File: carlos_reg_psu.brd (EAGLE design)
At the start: 51.7 x 40.6 mm, 17 parts

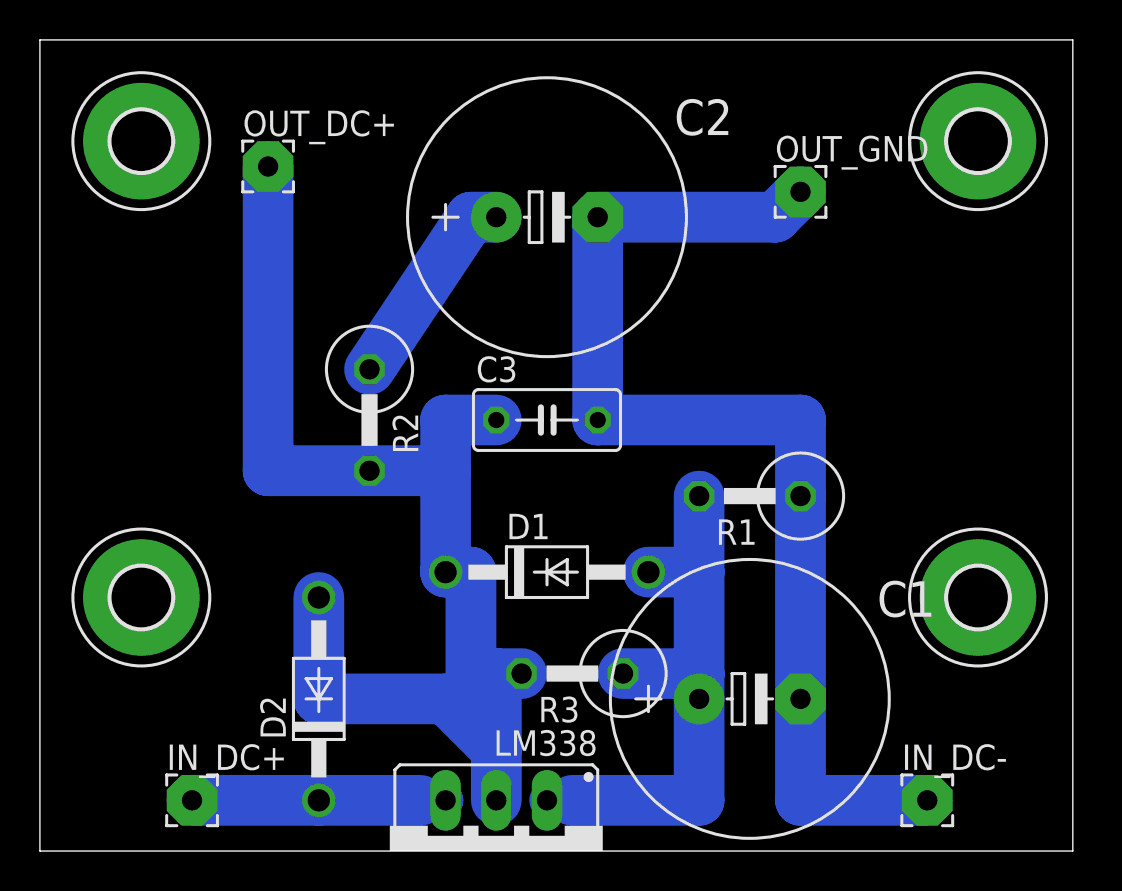
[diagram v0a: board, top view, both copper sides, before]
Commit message: minor placement fix
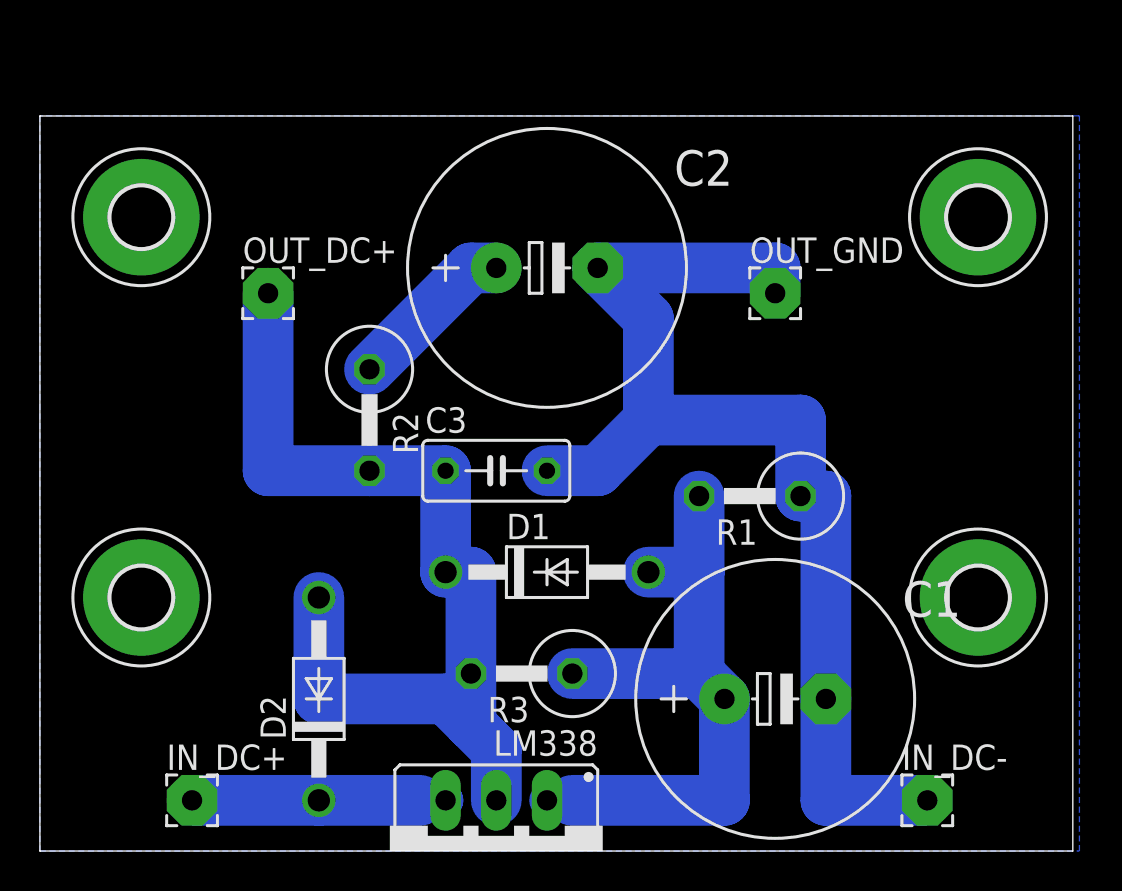
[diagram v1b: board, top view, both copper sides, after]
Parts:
- moved OUT_DC+ 6.35 mm to (11.4, 27.9)
- moved OUT_GND 5.24 mm to (36.8, 27.9)
- moved H3 3.81 mm to (47.0, 31.8)
- moved H4 3.81 mm to (5.08, 31.8)
- moved C3 3.59 mm to (22.9, 19.1)
- moved R3 2.54 mm to (24.1, 8.89)
- moved C2 2.54 mm to (25.4, 29.2)
- moved C1 1.27 mm to (36.8, 7.62)
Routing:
- net N$3: track 64.6 -> 49.3 mm
- net N$2: track 29.2 -> 33.5 mm
- net N$1: track 10.4 -> 8.45 mm
- net N$6: track 56.4 -> 58.0 mm
- added copper zone on layer 16, net GND
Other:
- board size 51.7 x 40.6 mm -> 51.7 x 36.8 mm
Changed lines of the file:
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@@
 <plain>
 <wire x1="0" y1="0" x2="51.74" y2="0" width="0" layer="20"/>
-<wire x1="51.74" y1="0" x2="51.74" y2="40.63" width="0" layer="20"/>
-<wire x1="51.74" y1="40.63" x2="0" y2="40.63" width="0" layer="20"/>
-<wire x1="0" y1="40.63" x2="0" y2="0" width="0" layer="20"/>
+<wire x1="51.74" y1="0" x2="51.74" y2="36.82" width="0" layer="20"/>
+<wire x1="51.74" y1="36.82" x2="0" y2="36.82" width="0" layer="20"/>
+<wire x1="0" y1="36.82" x2="0" y2="0" width="0" layer="20"/>
 </plain>
 <attributes>
@@
 </autorouter>
 <elements>
-<element name="C1" library="resistor" package="E5-13" value="47uF" x="35.56" y="7.62"/>
-<element name="C2" library="resistor" package="E5-13" value="47uF" x="25.4" y="31.75"/>
-<element name="C3" library="rcl" package="C050-030X075" value="47nF" x="25.4" y="21.59"/>
+<element name="C1" library="resistor" package="E5-13" value="47uF" x="36.83" y="7.62"/>
+<element name="C2" library="resistor" package="E5-13" value="47uF" x="25.4" y="29.21"/>
+<element name="C3" library="rcl" package="C050-030X075" value="47nF" x="22.86" y="19.05"/>
 <element name="D1" library="diode" package="DO41-10" value="1N4002" x="25.4" y="13.97"/>
 <element name="D2" library="diode" package="DO41-10" value="1N4002" x="13.97" y="7.62" rot="R90"/>
@@
 <element name="IN_DC-" library="wirepad" package="2,54/1,0" value="" x="44.45" y="2.54"/>
 <element name="LM338" library="v-reg" package="317TS" value="" x="22.86" y="0" rot="R180"/>
-<element name="OUT_DC+" library="wirepad" package="2,54/1,0" value="" x="11.43" y="34.29"/>
-<element name="OUT_GND" library="wirepad" package="2,54/1,0" value="" x="38.1" y="33.02"/>
+<element name="OUT_DC+" library="wirepad" package="2,54/1,0" value="" x="11.43" y="27.94"/>
+<element name="OUT_GND" library="wirepad" package="2,54/1,0" value="" x="36.83" y="27.94"/>
 <element name="R1" library="resistor" package="0414V" value="2k2" x="35.56" y="17.78" rot="R180"/>
 <element name="R2" library="resistor" package="0414V" value="0.47R" x="16.51" y="21.59" rot="R270"/>
-<element name="R3" library="resistor" package="0414V" value="91R" x="26.67" y="8.89" rot="R180"/>
+<element name="R3" library="resistor" package="0414V" value="91R" x="24.13" y="8.89" rot="R180"/>
 <element name="H1" library="holes" package="3,0-PAD" value="MOUNT-PAD-ROUND3.0" x="46.99" y="12.7"/>
 <element name="H2" library="holes" package="3,0-PAD" value="MOUNT-PAD-ROUND3.0" x="5.08" y="12.7"/>
-<element name="H3" library="holes" package="3,0-PAD" value="MOUNT-PAD-ROUND3.0" x="46.99" y="35.56"/>
-<element name="H4" library="holes" package="3,0-PAD" value="MOUNT-PAD-ROUND3.0" x="5.08" y="35.56"/>
+<element name="H3" library="holes" package="3,0-PAD" value="MOUNT-PAD-ROUND3.0" x="46.99" y="31.75"/>
+<element name="H4" library="holes" package="3,0-PAD" value="MOUNT-PAD-ROUND3.0" x="5.08" y="31.75"/>
 </elements>
 <signals>
@@
 <contactref element="C1" pad="+"/>
 <contactref element="D1" pad="A"/>
-<wire x1="33.02" y1="7.62" x2="33.02" y2="2.54" width="2.54" layer="16"/>
-<wire x1="33.02" y1="2.54" x2="26.67" y2="2.54" width="2.54" layer="16"/>
+<wire x1="34.29" y1="7.62" x2="34.29" y2="2.54" width="2.54" layer="16"/>
+<wire x1="34.29" y1="2.54" x2="26.67" y2="2.54" width="2.54" layer="16"/>
 <wire x1="25.4" y1="2.54" x2="26.67" y2="2.54" width="1.778" layer="16"/>
 <wire x1="33.02" y1="17.78" x2="33.02" y2="13.97" width="2.54" layer="16"/>
 <wire x1="33.02" y1="13.97" x2="33.02" y2="8.89" width="2.54" layer="16"/>
-<wire x1="33.02" y1="8.89" x2="33.02" y2="7.62" width="2.54" layer="16"/>
-<wire x1="29.21" y1="8.89" x2="33.02" y2="8.89" width="2.54" layer="16"/>
+<wire x1="33.02" y1="8.89" x2="34.29" y2="7.62" width="2.54" layer="16"/>
+<wire x1="26.67" y1="8.89" x2="33.02" y2="8.89" width="2.54" layer="16"/>
 <wire x1="30.48" y1="13.97" x2="33.02" y2="13.97" width="2.54" layer="16"/>
 </signal>
@@
 <wire x1="13.97" y1="12.7" x2="13.97" y2="7.62" width="2.54" layer="16"/>
 <wire x1="13.97" y1="7.62" x2="20.32" y2="7.62" width="2.54" layer="16"/>
-<wire x1="20.32" y1="7.62" x2="22.86" y2="5.08" width="2.54" layer="16"/>
+<wire x1="20.32" y1="7.62" x2="21.59" y2="6.35" width="2.54" layer="16"/>
+<wire x1="21.59" y1="6.35" x2="22.86" y2="5.08" width="2.54" layer="16"/>
 <wire x1="22.86" y1="5.08" x2="22.86" y2="2.54" width="2.54" layer="16"/>
 <contactref element="R3" pad="2"/>
-<wire x1="24.13" y1="8.89" x2="22.86" y2="8.89" width="2.54" layer="16"/>
-<wire x1="22.86" y1="8.89" x2="22.86" y2="5.08" width="2.54" layer="16"/>
 <wire x1="20.32" y1="13.97" x2="21.59" y2="13.97" width="2.54" layer="16"/>
-<wire x1="21.59" y1="13.97" x2="21.59" y2="7.62" width="2.54" layer="16"/>
-<wire x1="22.86" y1="21.59" x2="20.32" y2="21.59" width="2.54" layer="16"/>
-<wire x1="20.32" y1="21.59" x2="20.32" y2="19.05" width="2.54" layer="16"/>
+<wire x1="20.32" y1="21.59" x2="20.32" y2="19.05" width="0" layer="19" extent="1-16"/>
 <wire x1="20.32" y1="19.05" x2="20.32" y2="13.97" width="2.54" layer="16"/>
 <wire x1="16.51" y1="19.05" x2="20.32" y2="19.05" width="2.54" layer="16"/>
 <wire x1="11.43" y1="19.05" x2="16.51" y2="19.05" width="2.54" layer="16"/>
-<wire x1="11.43" y1="19.05" x2="11.43" y2="34.29" width="2.54" layer="16"/>
-<wire x1="20.32" y1="7.62" x2="21.59" y2="7.62" width="0" layer="19" extent="16-16"/>
+<wire x1="21.59" y1="13.97" x2="21.59" y2="6.35" width="2.54" layer="16"/>
+<wire x1="20.32" y1="7.62" x2="21.59" y2="8.89" width="0" layer="19" extent="16-16"/>
+<wire x1="11.43" y1="27.94" x2="11.43" y2="19.05" width="2.54" layer="16"/>
 </signal>
 <signal name="N$4">
@@
 <contactref element="IN_DC-" pad="1"/>
 <contactref element="OUT_GND" pad="1"/>
-<wire x1="38.1" y1="7.62" x2="38.1" y2="2.54" width="2.54" layer="16"/>
-<wire x1="38.1" y1="2.54" x2="44.45" y2="2.54" width="2.54" layer="16"/>
-<wire x1="38.1" y1="7.62" x2="38.1" y2="17.78" width="2.54" layer="16"/>
+<wire x1="39.37" y1="7.62" x2="39.37" y2="2.54" width="2.54" layer="16"/>
+<wire x1="39.37" y1="2.54" x2="44.45" y2="2.54" width="2.54" layer="16"/>
 <wire x1="38.1" y1="17.78" x2="38.1" y2="21.59" width="2.54" layer="16"/>
-<wire x1="38.1" y1="21.59" x2="27.94" y2="21.59" width="2.54" layer="16"/>
-<wire x1="27.94" y1="31.75" x2="27.94" y2="21.59" width="2.54" layer="16"/>
-<wire x1="38.1" y1="33.02" x2="36.83" y2="31.75" width="2.54" layer="16"/>
-<wire x1="36.83" y1="31.75" x2="27.94" y2="31.75" width="2.54" layer="16"/>
+<wire x1="39.37" y1="7.62" x2="39.37" y2="17.78" width="2.54" layer="16"/>
+<wire x1="39.37" y1="17.78" x2="38.1" y2="17.78" width="2.54" layer="16"/>
+<wire x1="38.1" y1="21.59" x2="30.48" y2="21.59" width="2.54" layer="16"/>
+<wire x1="30.48" y1="21.59" x2="27.94" y2="19.05" width="2.54" layer="16"/>
+<wire x1="27.94" y1="19.05" x2="25.4" y2="19.05" width="2.54" layer="16"/>
+<wire x1="27.94" y1="29.21" x2="30.48" y2="26.67" width="2.54" layer="16"/>
+<wire x1="30.48" y1="26.67" x2="30.48" y2="21.59" width="2.54" layer="16"/>
+<wire x1="36.83" y1="27.94" x2="36.83" y2="29.21" width="2.54" layer="16"/>
+<wire x1="36.83" y1="29.21" x2="27.94" y2="29.21" width="2.54" layer="16"/>
 </signal>
 <signal name="N$1">
 <contactref element="C2" pad="+"/>
 <contactref element="R2" pad="1"/>
-<wire x1="16.51" y1="24.13" x2="21.59" y2="31.75" width="2.54" layer="16"/>
-<wire x1="21.59" y1="31.75" x2="22.86" y2="31.75" width="2.54" layer="16"/>
+<wire x1="16.51" y1="24.13" x2="21.59" y2="29.21" width="2.54" layer="16"/>
+<wire x1="21.59" y1="29.21" x2="22.86" y2="29.21" width="2.54" layer="16"/>
+</signal>
+<signal name="GND">
+<polygon width="1.27" layer="16" isolate="1.27">
+<vertex x="0" y="0"/>
+<vertex x="52.07" y="0"/>
+<vertex x="52.07" y="36.83"/>
+<vertex x="0" y="36.83"/>
+</polygon>
 </signal>
 </signals>

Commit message: moved current set resistor closer to output as described in datasheet
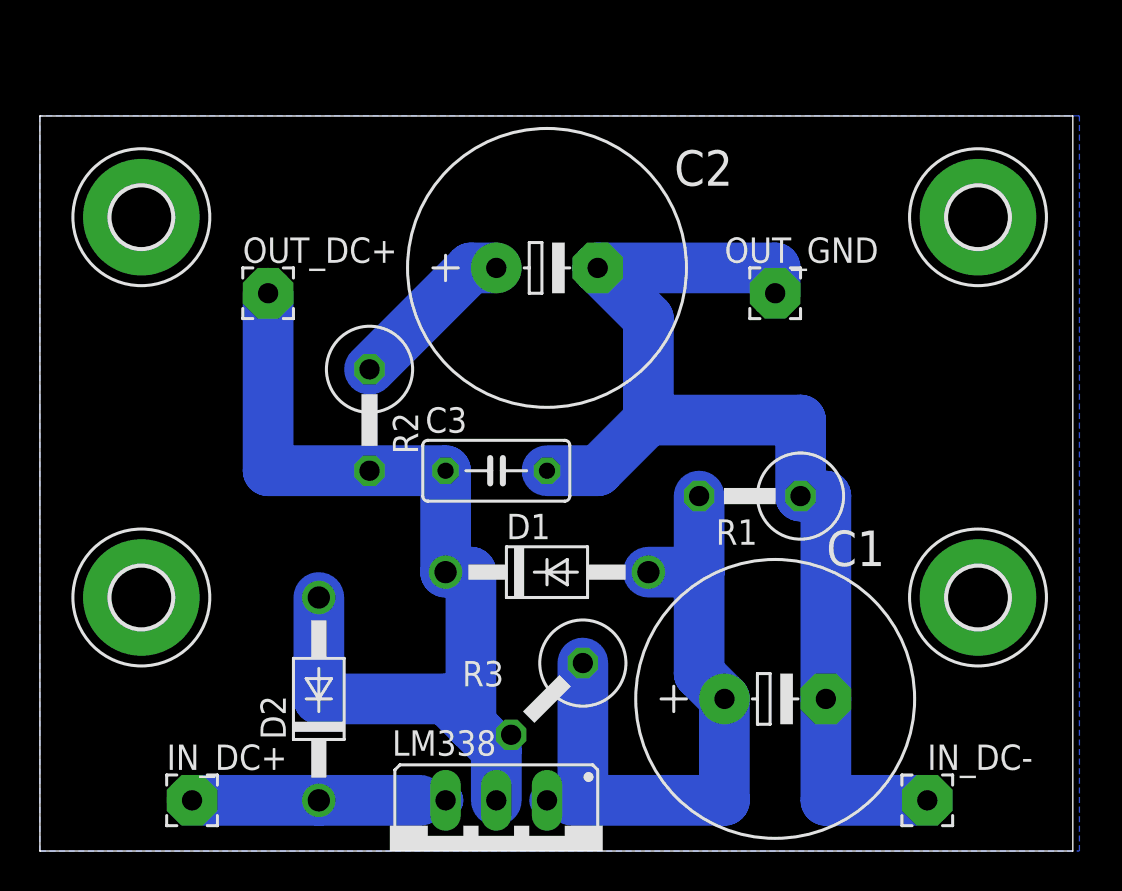
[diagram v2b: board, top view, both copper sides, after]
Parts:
- moved R3 1.80 mm to (25.4, 7.62), turned to 225 degrees
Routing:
- net N$3: track 49.3 -> 50.4 mm
- net N$2: track 33.5 -> 34.4 mm
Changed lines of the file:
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@@
 <layer number="43" name="vRestrict" color="2" fill="10" visible="yes" active="yes"/>
 <layer number="44" name="Drills" color="7" fill="1" visible="no" active="yes"/>
-<layer number="45" name="Holes" color="7" fill="1" visible="no" active="yes"/>
+<layer number="45" name="Holes" color="7" fill="1" visible="yes" active="yes"/>
 <layer number="46" name="Milling" color="3" fill="1" visible="no" active="yes"/>
 <layer number="47" name="Measures" color="7" fill="1" visible="no" active="yes"/>
@@
 </autorouter>
 <elements>
-<element name="C1" library="resistor" package="E5-13" value="47uF" x="36.83" y="7.62"/>
+<element name="C1" library="resistor" package="E5-13" value="47uF" x="36.83" y="7.62" smashed="yes">
+<attribute name="NAME" x="39.3954" y="14.2748" size="1.778" layer="25" ratio="10"/>
+<attribute name="VALUE" x="32.258" y="3.683" size="1.778" layer="27" ratio="10"/>
+</element>
 <element name="C2" library="resistor" package="E5-13" value="47uF" x="25.4" y="29.21"/>
 <element name="C3" library="rcl" package="C050-030X075" value="47nF" x="22.86" y="19.05"/>
-<element name="D1" library="diode" package="DO41-10" value="1N4002" x="25.4" y="13.97"/>
+<element name="D1" library="diode" package="DO41-10" value="1N4002" x="25.4" y="13.97" smashed="yes">
+<attribute name="NAME" x="23.368" y="15.621" size="1.27" layer="25" ratio="10"/>
+<attribute name="VALUE" x="19.558" y="11.176" size="1.27" layer="27" ratio="10"/>
+</element>
 <element name="D2" library="diode" package="DO41-10" value="1N4002" x="13.97" y="7.62" rot="R90"/>
 <element name="IN_DC+" library="wirepad" package="2,54/1,0" value="" x="7.62" y="2.54"/>
-<element name="IN_DC-" library="wirepad" package="2,54/1,0" value="" x="44.45" y="2.54"/>
-<element name="LM338" library="v-reg" package="317TS" value="" x="22.86" y="0" rot="R180"/>
+<element name="IN_DC-" library="wirepad" package="2,54/1,0" value="" x="44.45" y="2.54" smashed="yes">
+<attribute name="NAME" x="44.45" y="4.064" size="1.27" layer="25" ratio="10"/>
+<attribute name="VALUE" x="44.45" y="3.54" size="0.0254" layer="27"/>
+</element>
+<element name="LM338" library="v-reg" package="317TS" value="" x="22.86" y="0" smashed="yes" rot="R180">
+<attribute name="NAME" x="22.86" y="6.0452" size="1.27" layer="25" ratio="10" rot="R180"/>
+<attribute name="VALUE" x="27.94" y="7.62" size="1.27" layer="27" ratio="10" rot="R180"/>
+</element>
 <element name="OUT_DC+" library="wirepad" package="2,54/1,0" value="" x="11.43" y="27.94"/>
-<element name="OUT_GND" library="wirepad" package="2,54/1,0" value="" x="36.83" y="27.94"/>
+<element name="OUT_GND" library="wirepad" package="2,54/1,0" value="" x="36.83" y="27.94" smashed="yes">
+<attribute name="NAME" x="34.29" y="29.464" size="1.27" layer="25" ratio="10"/>
+<attribute name="VALUE" x="36.83" y="28.94" size="0.0254" layer="27"/>
+</element>
 <element name="R1" library="resistor" package="0414V" value="2k2" x="35.56" y="17.78" rot="R180"/>
 <element name="R2" library="resistor" package="0414V" value="0.47R" x="16.51" y="21.59" rot="R270"/>
-<element name="R3" library="resistor" package="0414V" value="91R" x="24.13" y="8.89" rot="R180"/>
+<element name="R3" library="resistor" package="0414V" value="91R" x="25.4" y="7.62" smashed="yes" rot="R225">
+<attribute name="NAME" x="23.240996875" y="9.51765" size="1.27" layer="25" ratio="10" rot="R180"/>
+<attribute name="VALUE" x="23.240996875" y="8.186146875" size="1.27" layer="27" ratio="10" rot="R180"/>
+</element>
 <element name="H1" library="holes" package="3,0-PAD" value="MOUNT-PAD-ROUND3.0" x="46.99" y="12.7"/>
 <element name="H2" library="holes" package="3,0-PAD" value="MOUNT-PAD-ROUND3.0" x="5.08" y="12.7"/>
@@
 <contactref element="D1" pad="A"/>
 <wire x1="34.29" y1="7.62" x2="34.29" y2="2.54" width="2.54" layer="16"/>
-<wire x1="34.29" y1="2.54" x2="26.67" y2="2.54" width="2.54" layer="16"/>
+<wire x1="34.29" y1="2.54" x2="27.94" y2="2.54" width="2.54" layer="16"/>
+<wire x1="27.94" y1="2.54" x2="26.67" y2="2.54" width="2.54" layer="16"/>
 <wire x1="25.4" y1="2.54" x2="26.67" y2="2.54" width="1.778" layer="16"/>
 <wire x1="33.02" y1="17.78" x2="33.02" y2="13.97" width="2.54" layer="16"/>
 <wire x1="33.02" y1="13.97" x2="33.02" y2="8.89" width="2.54" layer="16"/>
 <wire x1="33.02" y1="8.89" x2="34.29" y2="7.62" width="2.54" layer="16"/>
-<wire x1="26.67" y1="8.89" x2="33.02" y2="8.89" width="2.54" layer="16"/>
 <wire x1="30.48" y1="13.97" x2="33.02" y2="13.97" width="2.54" layer="16"/>
+<wire x1="27.19605" y1="9.41605" x2="27.19605" y2="3.28395" width="2.54" layer="16"/>
+<wire x1="27.19605" y1="3.28395" x2="27.94" y2="2.54" width="2.54" layer="16"/>
 </signal>
 <signal name="N$3">
@@
 <wire x1="13.97" y1="12.7" x2="13.97" y2="7.62" width="2.54" layer="16"/>
 <wire x1="13.97" y1="7.62" x2="20.32" y2="7.62" width="2.54" layer="16"/>
-<wire x1="20.32" y1="7.62" x2="21.59" y2="6.35" width="2.54" layer="16"/>
 <wire x1="21.59" y1="6.35" x2="22.86" y2="5.08" width="2.54" layer="16"/>
 <wire x1="22.86" y1="5.08" x2="22.86" y2="2.54" width="2.54" layer="16"/>
@@
 <wire x1="11.43" y1="19.05" x2="16.51" y2="19.05" width="2.54" layer="16"/>
 <wire x1="21.59" y1="13.97" x2="21.59" y2="6.35" width="2.54" layer="16"/>
-<wire x1="20.32" y1="7.62" x2="21.59" y2="8.89" width="0" layer="19" extent="16-16"/>
 <wire x1="11.43" y1="27.94" x2="11.43" y2="19.05" width="2.54" layer="16"/>
+<wire x1="20.32" y1="7.62" x2="21.59" y2="6.35" width="2.54" layer="16"/>
+<wire x1="22.86" y1="5.08" x2="23.07789375" y2="5.08" width="1.27" layer="16"/>
+<wire x1="23.07789375" y1="5.08" x2="23.603946875" y2="5.823946875" width="1.27" layer="16"/>
 </signal>
 <signal name="N$4">
